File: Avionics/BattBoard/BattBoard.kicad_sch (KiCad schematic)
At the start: 32 parts, among them J1 Screw_Terminal_01x01, J2 JST_PH_S2B-PH-SM4, J3 Screw_Terminal_01x02, J4 Screw_Terminal_01x02, J5 Screw_Terminal_01x02, J6 Screw_Terminal_01x02, Q1 IRF7458, Q2 IRF7458

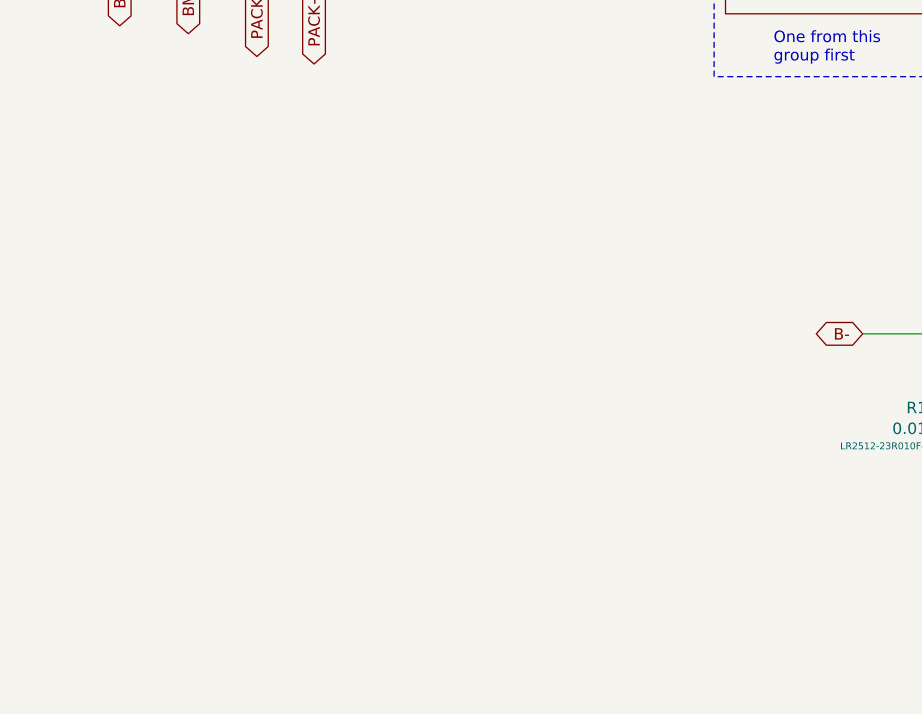
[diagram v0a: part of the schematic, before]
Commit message: Sephora Poteau: Added temperature sensor and terminal block connectors to Battery Board
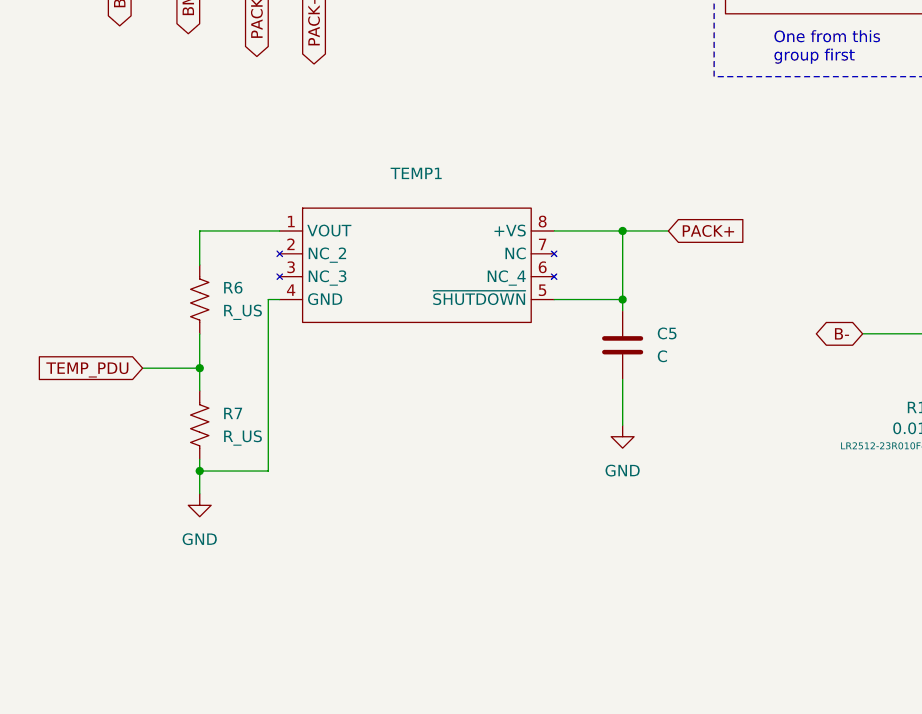
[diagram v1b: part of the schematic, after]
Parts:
- added C5: C, Capacitor_SMD:C_0603_1608Metric, symbol Device:C
- added R6, R7: R_US, Resistor_SMD:R_0603_1608Metric, symbol Device:R_US
- added TEMP1: ~, Sensor:Rohm_RPR-0521RS, symbol NewSymbols:TMP36FSZR_8_ADI-L
- H1, H2, H3, H4: footprint custom-footprints:MountingHole_3.2mm_M3_DIN965_PadMOD -> MountingHole:MountingHole_3.2mm_M3_DIN965_Pad
- J3, J4, J5, J6: footprint custom-footprints:SCREWTERMINAL-3.5MM-2_LOCK -> TerminalBlock:TerminalBlock_Altech_AK300-2_P5.00mm
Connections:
- net PACK+: now also C5.1, TEMP1.5 (~{SHUTDOWN}), TEMP1.8 (+VS)
- new net: R6.1, TEMP1.1 (VOUT)
- new net GND: C5.2, R7.2, TEMP1.4 (GND)
- new net TEMP_PDU: R6.2, R7.1
